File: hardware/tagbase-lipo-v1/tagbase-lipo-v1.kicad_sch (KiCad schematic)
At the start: 38 parts, among them J1 Conn_01x04_Female, J101 Conn_02x03_Odd_Even, J102 Conn_02x05_Odd_Even, J104 USB_B_Mini, J2 Conn_01x06, J5 Conn_01x02, SW1 SW_SPDT, SW2 SW_SPDT, U1 XC6206P332MR, U105 Tactile Switch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

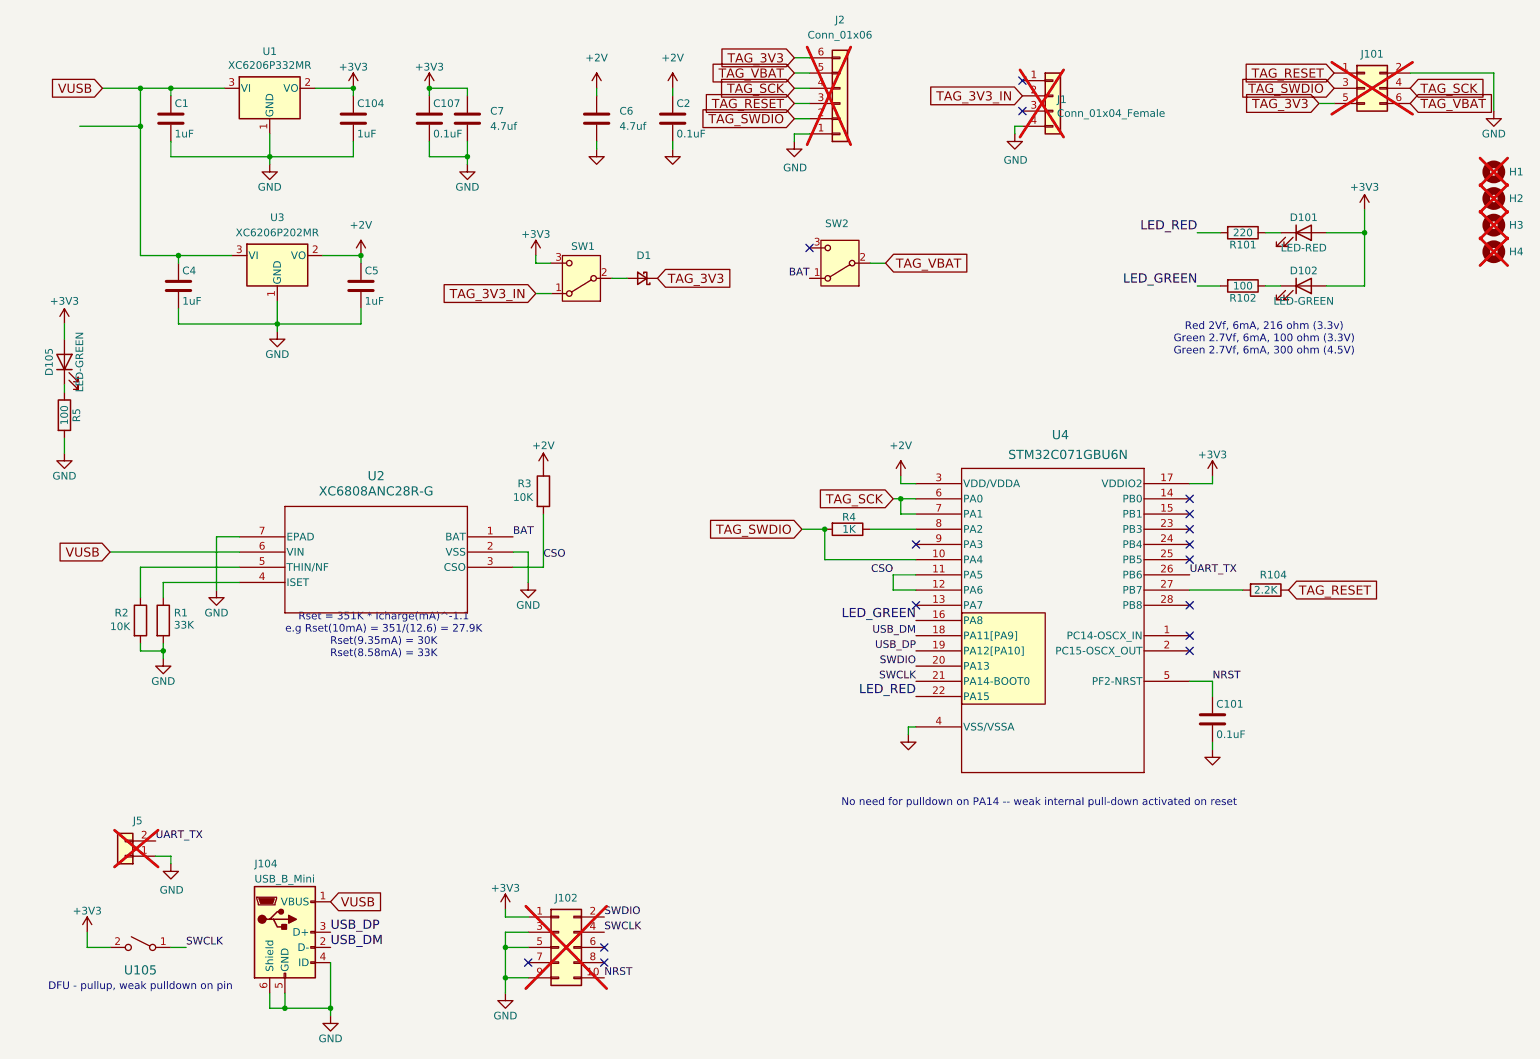
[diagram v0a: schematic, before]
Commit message: update tagbase lipo design
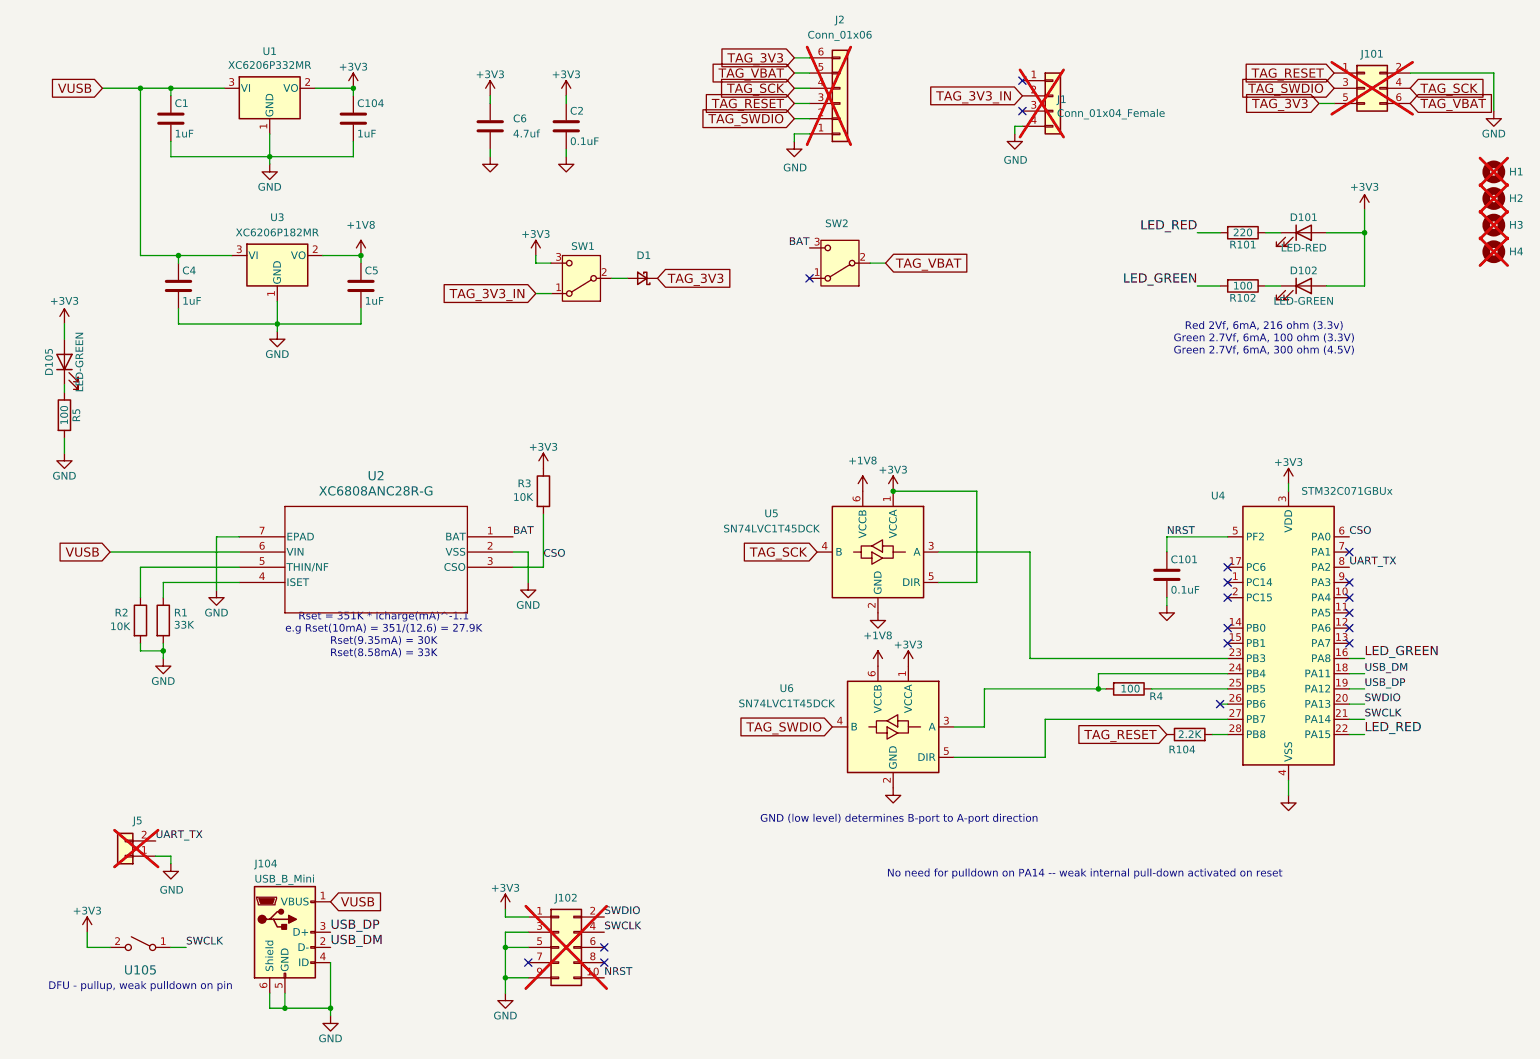
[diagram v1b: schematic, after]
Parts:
- removed C107: 0.1uF, Capacitor_SMD:C_0402_1005Metric, symbol Device:C
- removed C7: 4.7uf, Capacitor_SMD:C_0402_1005Metric, symbol Device:C
- removed U4: STM32C071GBU6N, UFQFPN-28_STM, symbol STM32C071GBU6N:STM32C071GBU6N
- added U4: STM32C071GBUx, Package_DFN_QFN:QFN-28_4x4mm_P0.5mm, symbol MCU_ST_STM32C0:STM32C071GBUx
- added U5, U6: SN74LVC1T45DCK, Package_TO_SOT_SMD:SOT-363_SC-70-6, symbol Logic_LevelTranslator:SN74LVC1T45DCK
- R4: value 1K -> 100; LCSC C11702 -> C25076; MPN 0402WGF1001TCE -> 0402WGF1000TCE
- U3: value XC6206P202MR -> XC6206P182MR; LCSC C2891260 -> C21659; MPN XC6206P202MR-G -> XC6206P182MR-G
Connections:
- net +3V3: now also C2.1, C6.1, R3.1, U4.3 (VDD), U5.1 (VCCA), U5.5 (DIR), U6.1 (VCCA)
- net BAT: now also SW2.3 (C); no longer SW2.1 (A)
- net CSO: now also U4.6 (PA0)
- net GND: now also U4.4 (VSS), U5.2 (GND), U6.2 (GND)
- net LED_GREEN: now also U4.16 (PA8)
- net LED_RED: now also U4.22 (PA15)
- net NRST: now also U4.5 (PF2)
- net SWCLK: now also U4.21 (PA14)
- net SWDIO: now also U4.20 (PA13)
- net TAG_SCK: now also U5.4 (B)
- net TAG_SWDIO: now also U6.4 (B); no longer R4.2
- net UART_TX: now also U4.8 (PA2)
- net USB_DM: now also U4.18 (PA11)
- net USB_DP: now also U4.19 (PA12)
- net at R104.2: now also U4.28 (PB8)
- net at R4.1: now also U4.25 (PB5)
- removed net +2V: C2.1, C5.1, C6.1, R3.1, U3.2 (VO)
- new net: R4.2, U4.24 (PB4), U6.3 (A)
- new net: U4.27 (PB7), U6.5 (DIR)
- new net: U4.23 (PB3), U5.3 (A)
- new net +1V8: C5.1, U3.2 (VO), U5.6 (VCCB), U6.6 (VCCB)
- no-connect marks 16 -> 18
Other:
- note added: "GND (low level) determines B-port to A-port direction"
- title: BitTag Base for JLCPCB fab  v7 -> Lipo Tag Base for JLCPCB --  V1
- moved on the sheet: C101, C2, C6, R104, R4

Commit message: added torpor tag
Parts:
- R4: footprint Resistor_SMD:R_0402_1005Metric -> Resistor_SMD:R_0603_1608Metric; LCSC C25076 -> C22775; MFN UNI-ROYAL(Uniroyal Elec) -> Uniroyal Elec.; MPN 0402WGF1000TCE -> 0603WAF1000T5E
- SW1, SW2: LCSC C132858 -> C35817163; MPN CJS-1201B -> CJS-1200B2
- U2: footprint USP-6B_TOR -> tagbase:xc6808
- U4: LCSC (none) -> C44521811; MFN (none) -> ST Microelectonics; MPN (none) -> STM32C071G8U6
- U5, U6: LCSC (none) -> C9382; MFN (none) -> TI; MPN (none) -> SN74LVC1T45DCKR
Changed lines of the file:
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@@
+			)
+		)
+		(property "LCSC" "C9382"
+			(at 158.75 135.89 0)
+			(effects
+				(font
+					(size 1.27 1.27)
+				)
+				(hide yes)
+			)
+		)
+		(property "MFN" "TI"
+			(at 158.75 135.89 0)
+			(effects
+				(font
+					(size 1.27 1.27)
+				)
+				(hide yes)
+			)
+		)
+		(property "MPN" "SN74LVC1T45DCKR"
+			(at 158.75 135.89 0)
+			(effects
+				(font
+					(size 1.27 1.27)
+				)
+				(hide yes)
 			)
 		)
@@
 			)
 		)
-		(property "MPN" "CJS-1201B"
+		(property "MPN" "CJS-1200B2"
 			(at 149.86 58.42 0)
 			(effects
@@
 			)
 		)
-		(property "LCSC" "C132858"
+		(property "LCSC" "C35817163"
 			(at 149.86 58.42 0)
 			(effects
@@
 			)
 		)
+		(property "LCSC" "C44521811"
+			(at 224.79 121.92 0)
+			(effects
+				(font
+					(size 1.27 1.27)
+				)
+				(hide yes)
+			)
+		)
+		(property "MFN" "ST Microelectonics"
+			(at 224.79 121.92 0)
+			(effects
+				(font
+					(size 1.27 1.27)
+				)
+				(hide yes)
+			)
+		)
+		(property "MPN" " STM32C071G8U6"
+			(at 224.79 121.92 0)
+			(effects
+				(font
+					(size 1.27 1.27)
+				)
+				(hide yes)
+			)
+		)
 		(pin "4"
 		)
@@
 		)
 		(property "Description" "Single-Bit Dual-Supply Bus Transceiver With Configurable Voltage Translation and 3-State Outputs, SOT-363"
+			(at 156.21 106.68 0)
+			(effects
+				(font
+					(size 1.27 1.27)
+				)
+				(hide yes)
+			)
+		)
+		(property "LCSC" "C9382"
+			(at 156.21 106.68 0)
+			(effects
+				(font
+					(size 1.27 1.27)
+				)
+				(hide yes)
+			)
+		)
+		(property "MFN" "TI"
+			(at 156.21 106.68 0)
+			(effects
+				(font
+					(size 1.27 1.27)
+				)
+				(hide yes)
+			)
+		)
+		(property "MPN" "SN74LVC1T45DCKR"
 			(at 156.21 106.68 0)
 			(effects
@@
 			)
 		)
-		(property "Footprint" "USP-6B_TOR"
+		(property "Footprint" "tagbase:xc6808"
 			(at 95.25 104.14 0)
 			(effects
@@
 				(path "/4d87b1cc-f1d4-4d5c-b687-12b1ff6c9e14"
 					(reference "U2")
+					(unit 1)
+				)
+			)
+		)
+	)
+	(symbol
+		(lib_id "Device:R")
+		(at 198.12 129.54 270)
+		(unit 1)
+		(exclude_from_sim no)
+		(in_bom yes)
+		(on_board yes)
+		(dnp no)
+		(property "Reference" "R4"
+			(at 198.12 131.572 90)
+			(effects
+				(font
+					(size 1.27 1.27)
+				)
+			)
+		)
+		(property "Value" "100"
+			(at 198.12 129.54 90)
+			(effects
+				(font
+					(size 1.27 1.27)
+				)
+			)
+		)
+		(property "Footprint" "Resistor_SMD:R_0603_1608Metric"
+			(at 198.12 127.762 90)
+			(effects
+				(font
+					(size 1.27 1.27)
+				)
+				(hide yes)
+			)
+		)
+		(property "Datasheet" ""
+			(at 198.12 129.54 0)
+			(effects
+				(font
+					(size 1.27 1.27)
+				)
+				(hide yes)
+			)
+		)
+		(property "Description" ""
+			(at 198.12 129.54 0)
+			(effects
+				(font
+					(size 1.27 1.27)
+				)
+				(hide yes)
+			)
+		)
+		(property "LCSC" "C22775"
+			(at 68.58 25.4 0)
+			(effects
+				(font
+					(size 1.27 1.27)
+				)
+				(hide yes)
+			)
+		)
+		(property "MFN" "Uniroyal Elec."
+			(at 68.58 25.4 0)
+			(effects
+				(font
+					(size 1.27 1.27)
+				)
+				(hide yes)
+			)
+		)
+		(property "MPN" "0603WAF1000T5E"
+			(at 68.58 25.4 0)
+			(effects
+				(font
+					(size 1.27 1.27)
+				)
+				(hide yes)
+			)
+		)
+		(pin "1"
+		)
+		(pin "2"
+		)
+		(instances
+			(project "tagbase-lipo-v1"
+				(path "/4d87b1cc-f1d4-4d5c-b687-12b1ff6c9e14"
+					(reference "R4")
 					(unit 1)
 				)
@@
 	)
 	(symbol
-		(lib_id "Device:R")
-		(at 198.12 129.54 270)
-		(unit 1)
-		(exclude_from_sim no)
-		(in_bom yes)
-		(on_board yes)
-		(dnp no)
-		(property "Reference" "R4"
-			(at 202.692 130.81 90)
-			(effects
-				(font
-					(size 1.27 1.27)
-				)
-			)
-		)
-		(property "Value" "100"
-			(at 198.374 129.54 90)
-			(effects
-				(font
-					(size 1.27 1.27)
-				)
-			)
-		)
-		(property "Footprint" "Resistor_SMD:R_0402_1005Metric"
-			(at 198.12 127.762 90)
-			(effects
-				(font
-					(size 1.27 1.27)
-				)
-				(hide yes)
-			)
-		)
-		(property "Datasheet" "~"
-			(at 198.12 129.54 0)
-			(effects
-				(font
-					(size 1.27 1.27)
-				)
-				(hide yes)
-			)
-		)
-		(property "Description" "Resistor"
-			(at 198.12 129.54 0)
-			(effects
-				(font
-					(size 1.27 1.27)
-				)
-				(hide yes)
-			)
-		)
-		(property "LCSC" "C25076"
-			(at 198.12 129.54 90)
-			(effects
-				(font
-					(size 1.27 1.27)
-				)
-				(hide yes)
-			)
-		)
-		(property "MFN" "UNI-ROYAL(Uniroyal Elec)"
-			(at 198.12 129.54 90)
-			(effects
-				(font
-					(size 1.27 1.27)
-				)
-				(hide yes)
-			)
-		)
-		(property "MPN" "0402WGF1000TCE"
-			(at 198.12 129.54 90)
-			(effects
-				(font
-					(size 1.27 1.27)
-				)
-				(hide yes)
-			)
-		)
-		(pin "2"
-		)
-		(pin "1"
-		)
-		(instances
-			(project ""
-				(path "/4d87b1cc-f1d4-4d5c-b687-12b1ff6c9e14"
-					(reference "R4")
-					(unit 1)
-				)
-			)
-		)
-	)
-	(symbol
 		(lib_id "Device:C")
 		(at 69.85 62.23 0)
@@
 			)
 		)
-		(property "MPN" "CJS-1201B"
+		(property "MPN" "CJS-1200B2"
 			(at 106.68 60.96 0)
 			(effects
@@
 			)
 		)
-		(property "LCSC" "C132858"
+		(property "LCSC" "C35817163"
 			(at 106.68 60.96 0)
 			(effects
